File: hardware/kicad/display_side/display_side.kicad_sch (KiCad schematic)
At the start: 30 parts, among them J1 RJ45, J2 EPD_FFC_24, J3 UART-DBG, J4 USB-OTG, U1 R-78E3.3-0.5, U2 SN65HVD3082E

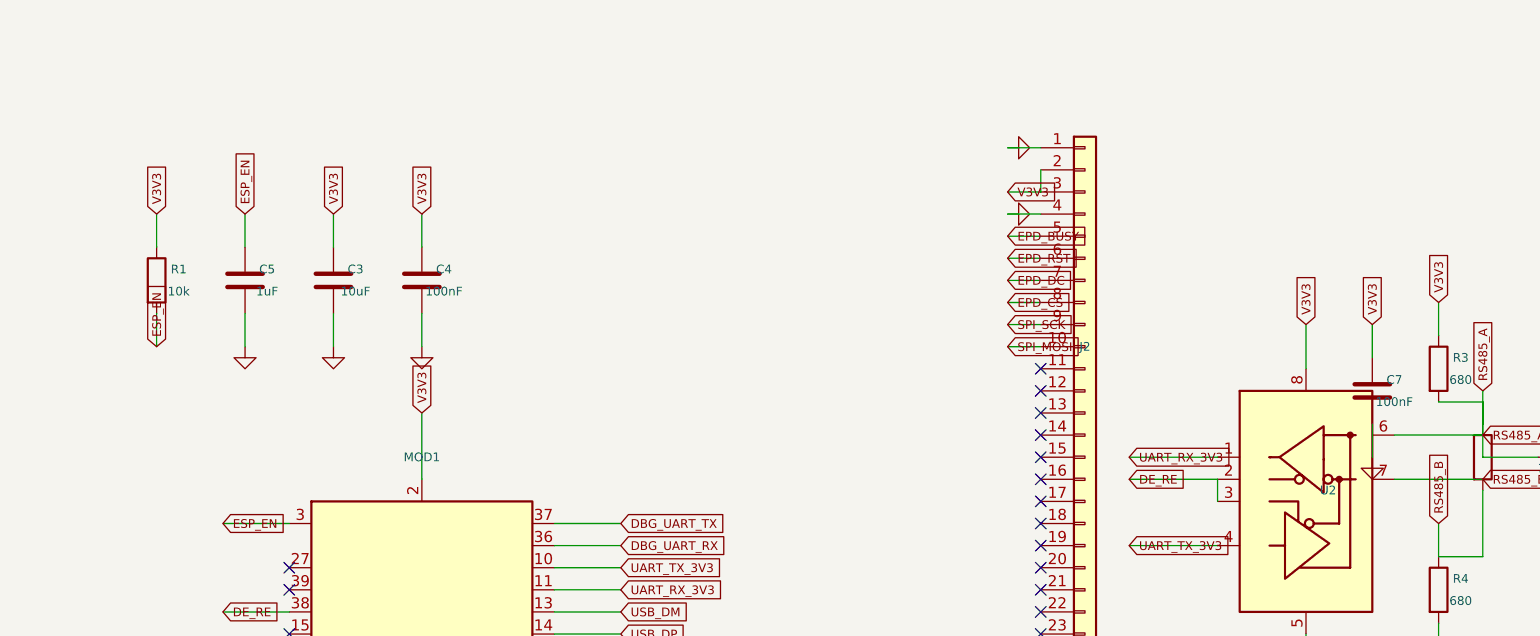
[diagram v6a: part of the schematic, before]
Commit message: review: CP6 iter-8 — more trunk wires: C10, C7, display support row
- C10 (U3 100nF VCC decoupling): V3V3_SW wired from C10.pin1 left
  to U3 pin 8 endpoint, then down to the existing label stub. U3
  keeps the single V3V3_SW label.
- C7 (U2 100nF VCC decoupling, display): same pattern — V3V3
  wired from C7.pin1 to U2 pin 8. U2 keeps the single label.
- Display ESP support row (R1 EN pull-up + C5 EN soft-start + C3
  10µF bulk + C4 100nF HF): V3V3 horizontal trunk added 2 G
  above the row, connecting R1.pin1, C3.pin1, C4.pin1. R1's
  V3V3 label is the single trunk label (was 3, now 1).

Audit: 0 pairs on both boards. ERC: 0 errors / 0 warnings.

Co-Authored-By: Claude Opus 4.7 (1M context) <noreply@anthropic.com>
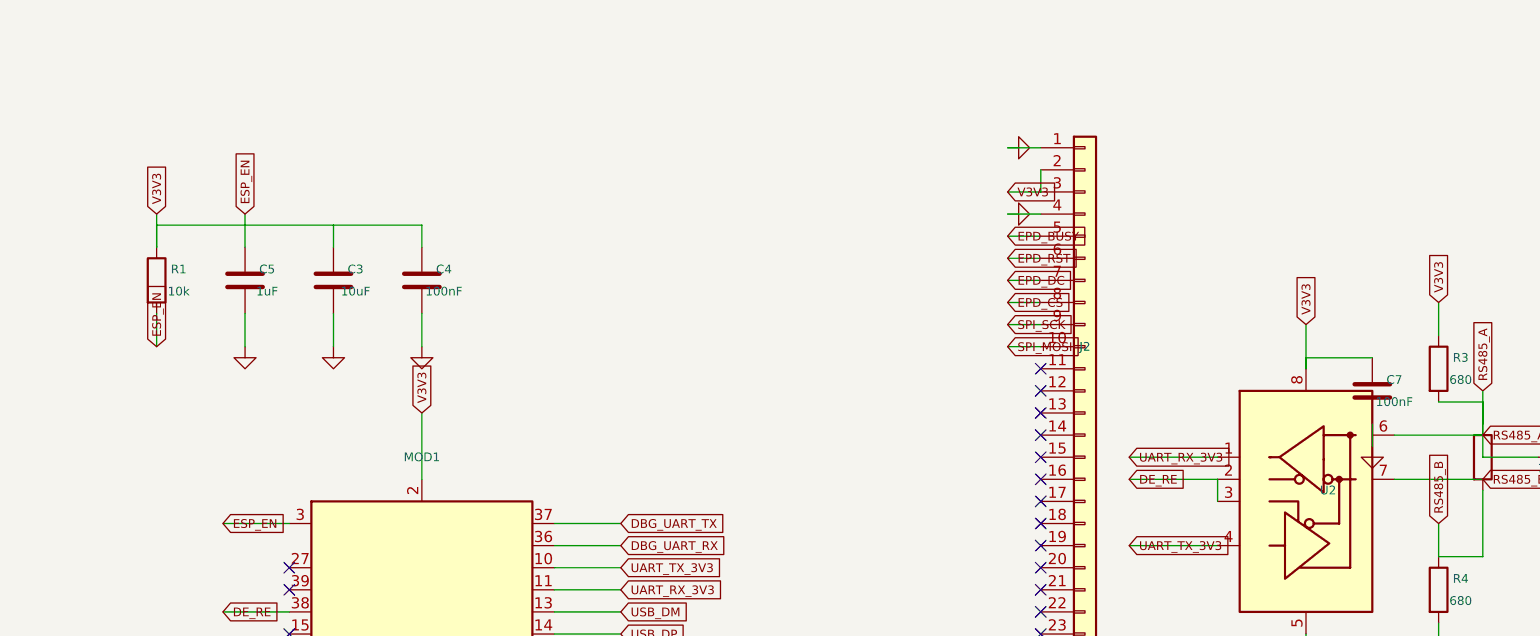
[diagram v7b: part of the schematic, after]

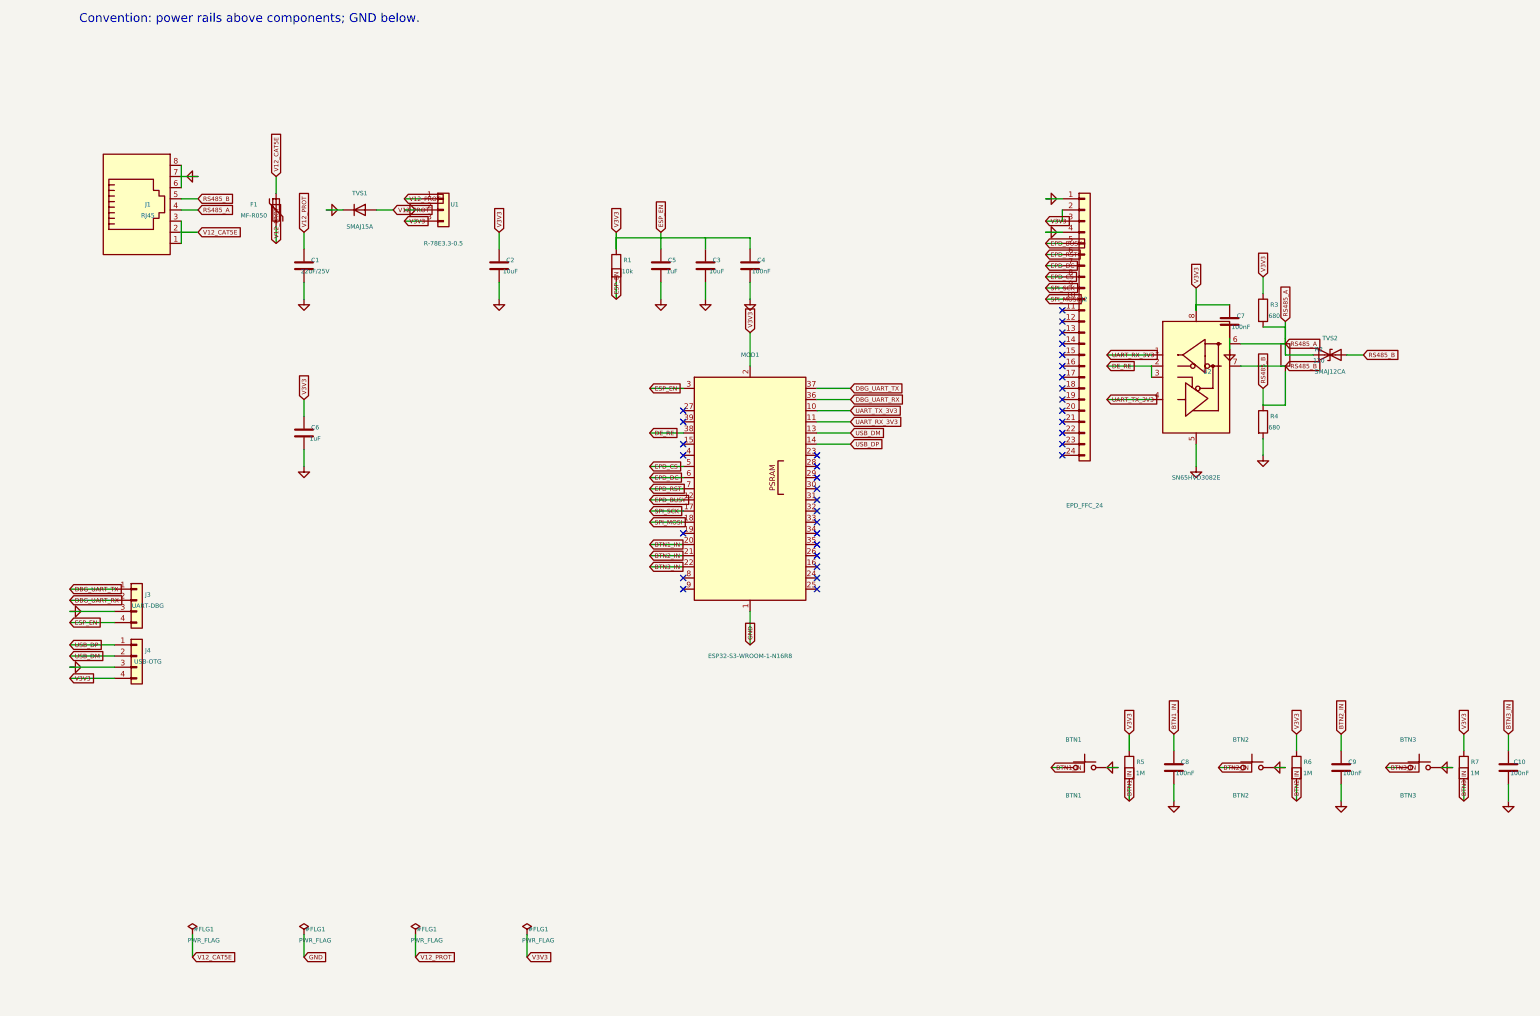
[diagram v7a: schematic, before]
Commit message: hardware: CP6 iter-9 — justify-based GlobalLabel orientation
The iter-8 fix used `shape=output` to flip the chevron for outdir=L/U
labels. That worked for chevron direction but left text positioning
ambiguous, and the label bodies still extended across pin numbers or
adjacent flags on the screenshots the user reviewed (J3 / J4 / U2 LEFT
side, BTN cluster, V12_PROT chain).

User feedback: "you can solve this mostly with the left/right text
justification settings — that gets the flag entry pointing the correct
direction AND gets the text inside the flag."

Per the empirical sweep documented in the chevron-direction memory:

  outdir | shape | justify_h | angle | result
  L      | input | right     |  0    | chevron-right (wire side), body left
  R      | input | left      |  0    | chevron-left (wire side), body right
  U      | input | left      | 90    | chevron-down (wire side), body up
  D      | input | right     | 90    | chevron-up (wire side), body down

Changes:
- `_place_label` now accepts `justify_h` and threads through Effects.
- `_pin_label` picks (angle, justify_h) from the outdir→combo map.
- Both connector loops (battery-side MOD1, display-side MOD1) compute
  the same map from (dx, dy) and use a longer 12G horizontal /
  8G vertical stub so chevron tips clear pin numbers on the wide
  ESP32-S3 module.
- Direct `_place_label` callers (U1 buck pins, Q1/Q2 MOSFET pins,
  RTC1, U3/U2 RS-485 chip pins, BTN cluster, conn loops, power-flag
  helper) all migrated to the new contract.

Overlap-reduction pass on top of that:
- TVS1 (battery) +20G right so V24_FUSED flag clears V24_AFTER_FUSE.
- U2 (display RS-485) +12G right so UART_*_3V3 label bodies clear
  J2's pin-15/16/19/20 numbers.
- U1 (display Recom buck) +10G right so V12_PROT label bodies clear
  U1's pin-number area.
- R10/R2 ref+value pulled further right to clear the widened
  RS485_A/B flag bodies.
- C_BST ref+value pulled further right to clear U1_BST flag body.
- C3 (battery V12 bulk) pulled -8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
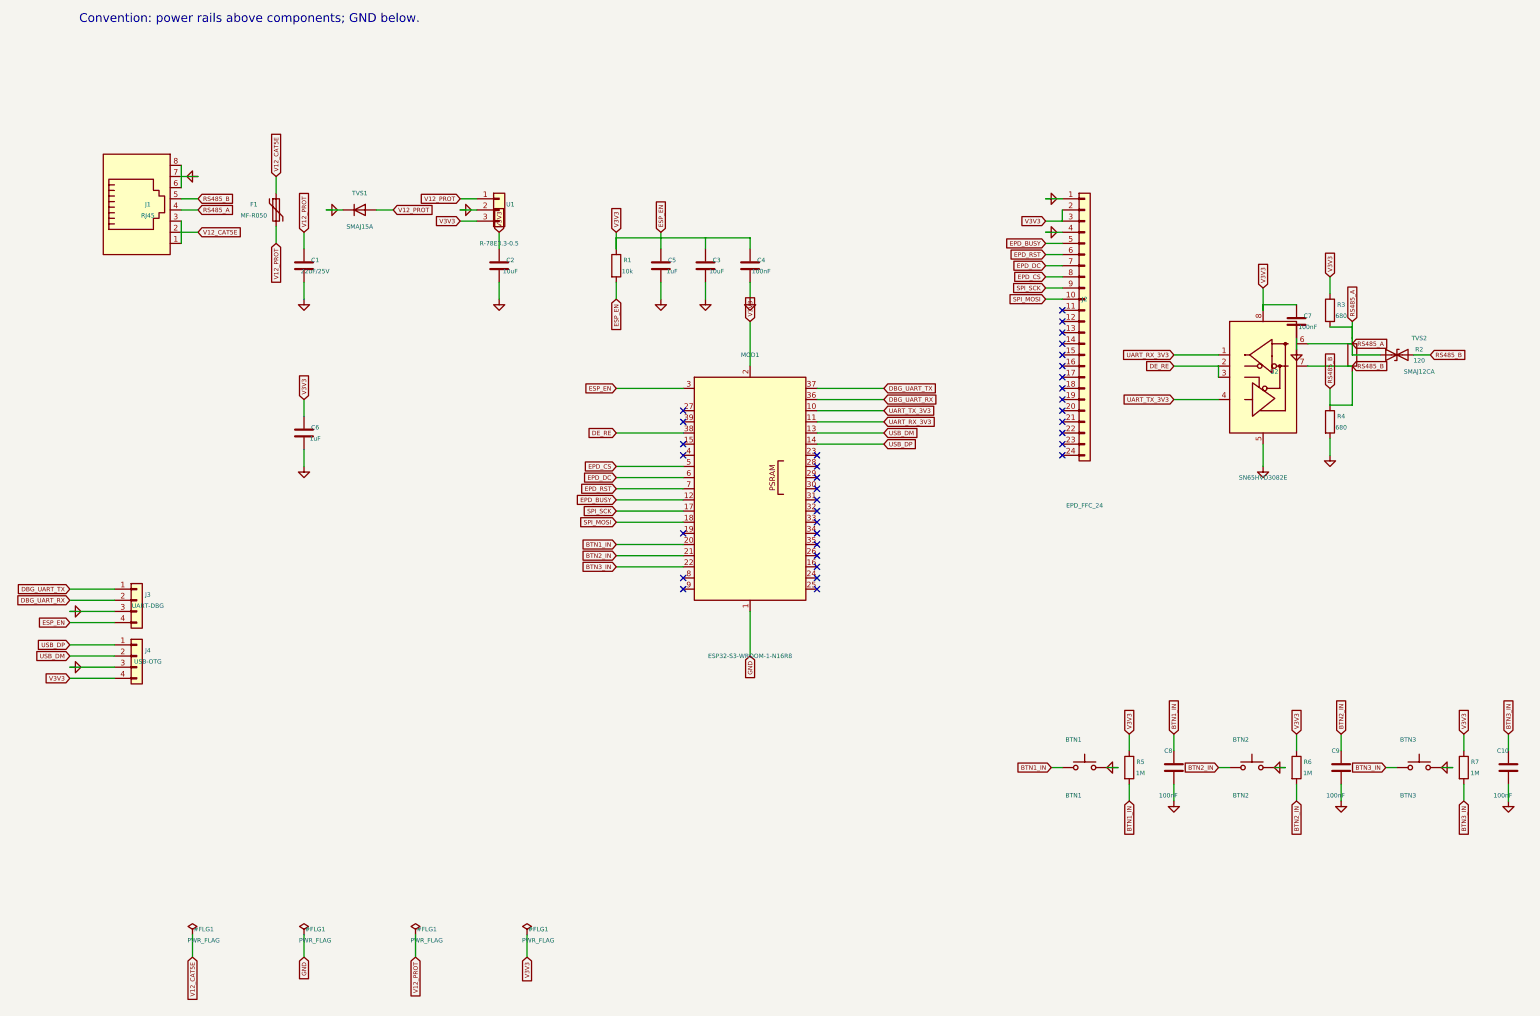
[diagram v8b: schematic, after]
